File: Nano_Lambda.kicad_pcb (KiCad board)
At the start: 2 copper layers, 22.2 x 47 mm, 70 parts, among them IC1 LMV321?M5, IC2 LM4041DBZ, J1 +12_IN, J10 PD3, J11 GP3, J12 DAC1, J13 DAC2, J14 Out1, J2 GND, J3 +12V_NL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

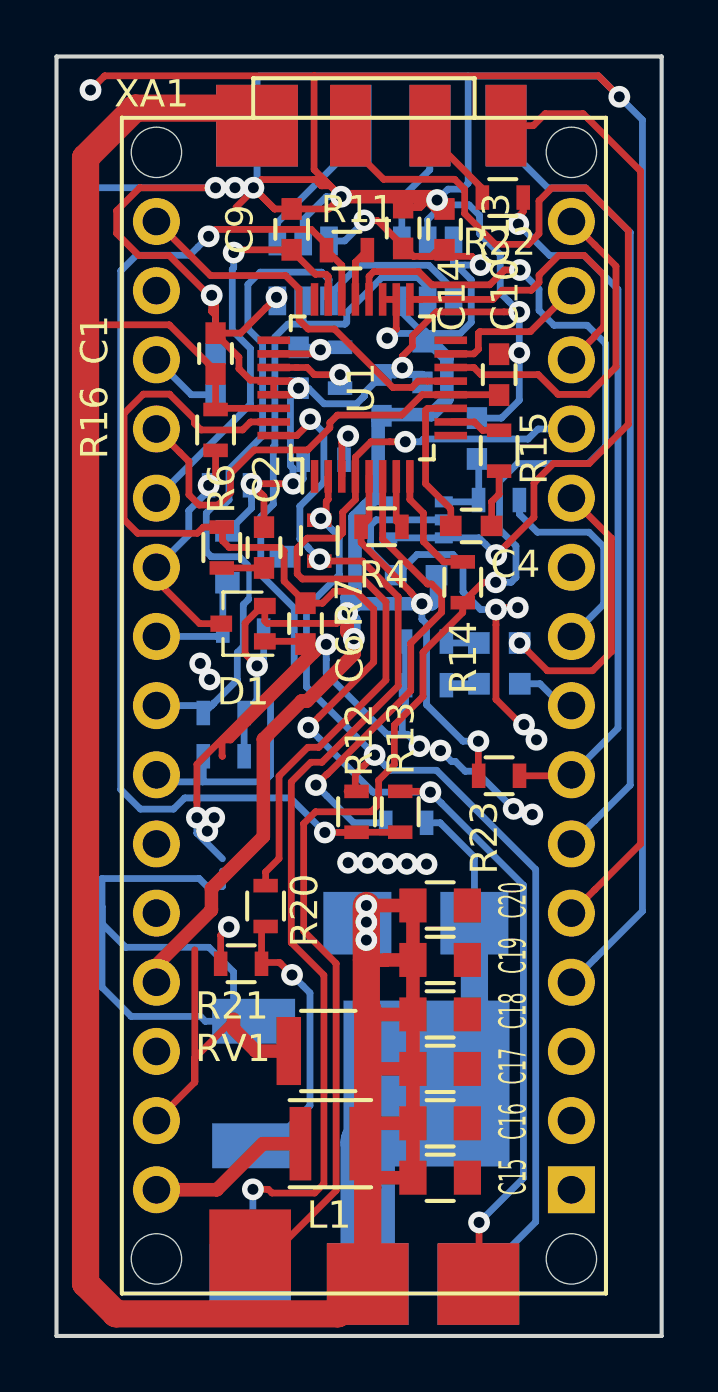
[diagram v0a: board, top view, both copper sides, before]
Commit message: Change to Version 0.9b
Changed wrong CJ125 Footprint to Footprint with 0.8mm pitch.
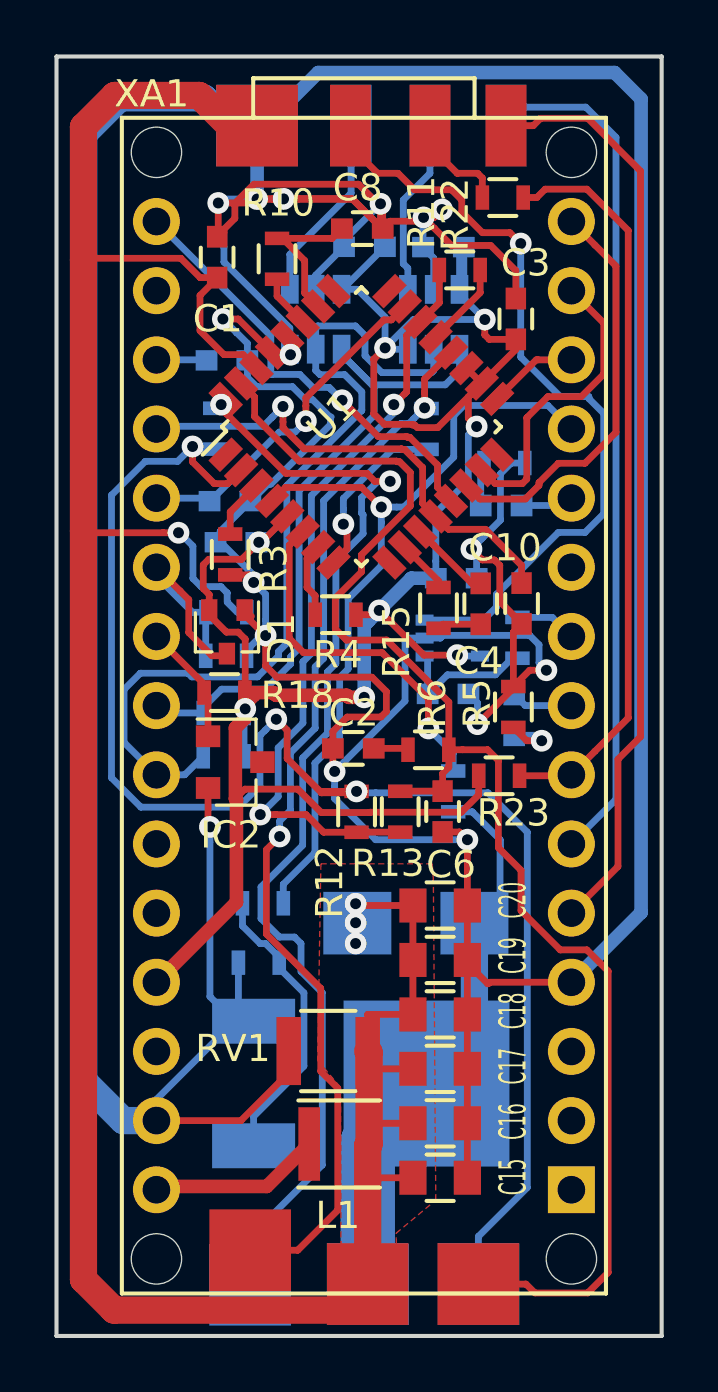
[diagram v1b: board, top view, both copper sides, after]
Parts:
- C13, C14, C9, R14, R16, R20, R21, R7: moved to B.Cu
- C3, C8, IC2, R10, R18, R3, R5: moved to F.Cu
- U1: footprint Housings_QFP:LQFP-32_5x5mm_Pitch0.5mm -> Housings_QFP:LQFP-32_7x7mm_Pitch0.8mm
- moved R6 10.6 mm to (173.7, 81.3), turned to 180 degrees
- moved C9 10.2 mm to (166.4, 72.2), turned to 0 degrees
- moved C5 9.53 mm to (166.6, 73.7), turned to 180 degrees
- moved C12 9.44 mm to (174.4, 79.3), turned to 180 degrees
- moved C6 8.54 mm to (174.2, 83.6)
- moved C10 8.45 mm to (177.1, 76.0), turned to 270 degrees
- moved C2 8.07 mm to (170.9, 81.3), turned to 180 degrees
- moved IC2 7.58 mm to (166.6, 81.8)
- moved R2 7.16 mm to (176.5, 70.8), turned to 180 degrees
- moved R16 6.71 mm to (166.3, 76.3), turned to 0 degrees
- moved R17 6.26 mm to (166.2, 77.9)
- moved R15 6.19 mm to (174.1, 76.1)
- moved R14 5.78 mm to (173.6, 69.6), turned to 90 degrees
- moved C3 5.67 mm to (176.9, 65.5)
- moved C8 5.62 mm to (171.2, 62.2), turned to 180 degrees
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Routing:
- net /IA: track 38.2 -> 57.0 mm, vias 2 -> 3
- net /VM: track 56.0 -> 39.4 mm
- net Net-(R11-Pad1): track 41.0 -> 28.1 mm
- net /LS_SS: track 11.8 -> 3.32 mm
- net /LED_1: track 10.4 -> 1.94 mm, vias 1 -> 0
- net +5V: track 79.5 -> 86.4 mm
- net /SDA: track 31.3 -> 25.2 mm
- net /WBL: track 8.27 -> 2.27 mm
- net /LS_MOSI: track 5.74 -> 11.2 mm
- net /Out1: track 34.1 -> 29.0 mm
- net /DIAHD: track 17.4 -> 13.2 mm
- net GND: track 256.7 -> 253.3 mm, vias 35 -> 16
- net /UA: track 15.5 -> 12.6 mm
- net Net-(C4-Pad1): track 5.58 -> 3.01 mm
- net Net-(C12-Pad2): track 2.83 -> 5.28 mm
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- added copper zone on F.Cu, net /+12V_NL
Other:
- board text added: "Nano Lambda Shield v0.9b 2018"
- board text removed: "Nano Lambda Shield v0.9 2018"

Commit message: Minor changes and new gerber files
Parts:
- moved C8 3.36 mm to (167.9, 62.2), turned to 225 degrees
- moved R14 1.37 mm to (173.5, 70.9)
- moved R11 0.69 mm to (174.5, 64.3), turned to 315 degrees
- moved R10 0.65 mm to (168.5, 63.8), turned to 225 degrees
- moved C1 0.36 mm to (165.6, 63.2)
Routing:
- net GND: track 253.3 -> 265.6 mm, vias 16 -> 20
- net +5V: track 86.4 -> 89.1 mm
- net /IA: track 57.0 -> 54.5 mm
- net /IP: track 42.3 -> 44.5 mm
- net Net-(C8-Pad2): track 5.77 -> 3.90 mm
- net Net-(R11-Pad2): track 3.15 -> 1.79 mm
- net /DIAHG: track 30.3 -> 31.1 mm
- net Net-(R11-Pad1): track 28.1 -> 27.6 mm
- net /UN: track 53.3 -> 53.9 mm

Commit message: Fabrication version 0.9b
Fabrication version 0.9b
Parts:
- moved C2 0.60 mm to (170.9, 81.9)
- moved R13 0.58 mm to (172.6, 84.2)
- moved R12 0.57 mm to (171.0, 84.2)
- moved R6 0.52 mm to (173.7, 81.9)
- moved C6 0.50 mm to (174.2, 84.1)
- moved R4 0.47 mm to (170.7, 76.4)
- moved C14 0.25 mm to (171.1, 62.9)
- turned D1 to 90 degrees
- turned R16 to 180 degrees
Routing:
- net GND: track 265.6 -> 333.0 mm, vias 20 -> 25
- net /IA: track 54.5 -> 47.7 mm, vias 3 -> 2
- net /+12V_NL: track 104.4 -> 100.9 mm
- net +5V: track 89.1 -> 90.6 mm, vias 8 -> 9
- net /UN: track 53.9 -> 55.0 mm
- net /SCL: track 33.2 -> 34.0 mm
- net /BRV: track 8.95 -> 9.59 mm

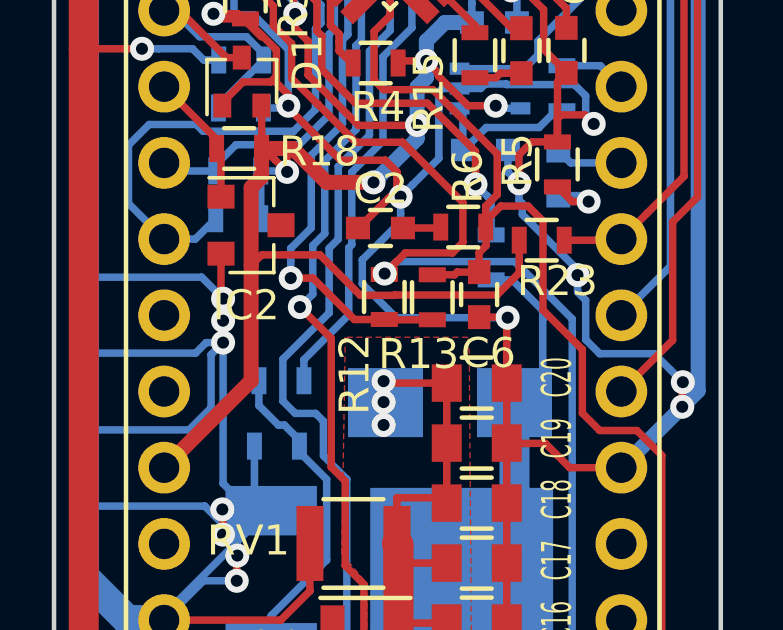
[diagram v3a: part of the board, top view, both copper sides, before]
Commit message: Diode u4 wrong direction
Swapped pin numbers on Diode MURS120 symbol in schematic. Changed pin 1
to 2 and 2 to 1
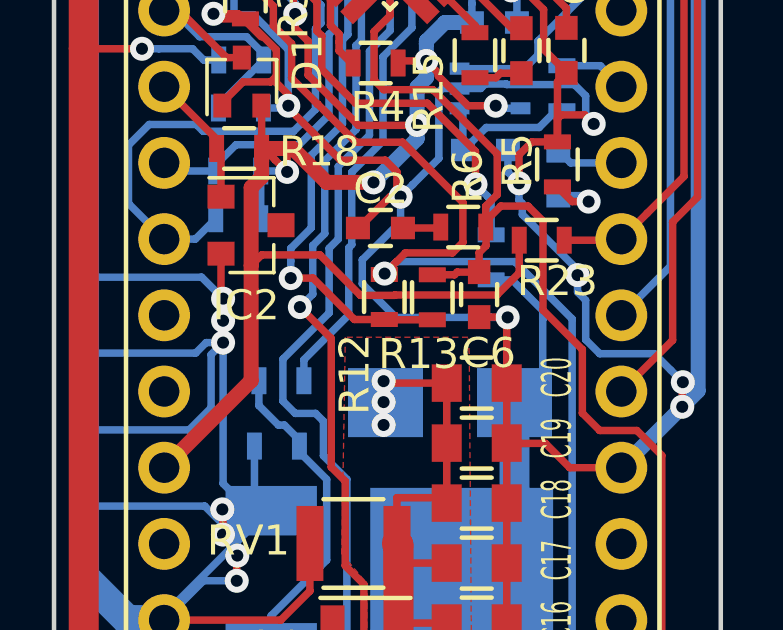
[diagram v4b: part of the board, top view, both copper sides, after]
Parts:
- turned U4 to 0 degrees
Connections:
- U4 pad 1: /NL_HEATER -> /+12V_NL
- U4 pad 2: /+12V_NL -> /NL_HEATER
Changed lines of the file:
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@@
   )
   (module Diodes_SMD:SMB_Standard (layer B.Cu)
-    (at 173.219 87.71 180)
+    (at 173.219 87.71)
     (descr "Diode SMB Standard")
     (tags "Diode SMB Standard")
     (attr smd)
-    (fp_text reference U4 (at -0.078 0.53 90) (layer B.SilkS)
-      (effects (font (size 1 1) (thickness 0.15)) (justify mirror))
-    )
-    (fp_text value MURS120 (at 0.05 -4.7 180) (layer B.Fab) hide
+    (fp_text reference U4 (at -0.078 0.53 -90) (layer B.SilkS)
+      (effects (font (size 1 1) (thickness 0.15)) (justify mirror))
+    )
+    (fp_text value MURS120 (at 0.05 -4.7) (layer B.Fab) hide
       (effects (font (size 1 1) (thickness 0.15)) (justify mirror))
     )
@@
     (fp_line (start 2.3 -2) (end -2.3 -2) (layer B.Fab) (width 0.1))
     (fp_line (start -3.55 2.15) (end -3.55 -2.15) (layer B.SilkS) (width 0.12))
-    (pad 2 smd rect (at 2.15 0 180) (size 2.5 2.3) (layers B.Cu B.Paste B.Mask)
-      (net 1 /+12V_NL))
-    (pad 1 smd rect (at -2.15 0 180) (size 2.5 2.3) (layers B.Cu B.Paste B.Mask)
+    (pad 2 smd rect (at 2.15 0) (size 2.5 2.3) (layers B.Cu B.Paste B.Mask)
       (net 24 /NL_HEATER))
+    (pad 1 smd rect (at -2.15 0) (size 2.5 2.3) (layers B.Cu B.Paste B.Mask)
+      (net 1 /+12V_NL))
     (model Diodes_SMD.3dshapes/SMB_Standard.wrl
       (at (xyz 0 0 0))
@@
   (segment (start 167.754301 77.89) (end 167.830001 77.8143) (width 0.25) (layer B.Cu) (net 2))
   (segment (start 166.02 74.78) (end 166.665685 74.78) (width 0.25) (layer B.Cu) (net 2))
-  (via (at 175.14 84.88) (size 0.8) (drill 0.4) (layers F.Cu B.Cu) (net 2))
-  (segment (start 175.11 87.06) (end 175.11 84.91) (width 0.25) (layer F.Cu) (net 2))
-  (segment (start 175.11 84.91) (end 175.14 84.88) (width 0.25) (layer F.Cu) (net 2))
-  (segment (start 175.12 84.86) (end 175.14 84.88) (width 0.25) (layer F.Cu) (net 2))
-  (segment (start 174.19 84.86) (end 175.12 84.86) (width 0.25) (layer F.Cu) (net 2))
   (segment (start 171.443005 80.589999) (end 171.443005 80.72869) (width 0.25) (layer F.Cu) (net 2))
   (via (at 171.573077 80.845367) (size 0.8) (drill 0.4) (layers F.Cu B.Cu) (net 2))
@@
   (segment (start 169.57 79.63) (end 167.7 77.76) (width 0.25) (layer F.Cu) (net 2))
   (segment (start 171.443005 80.589999) (end 171.45 80.583004) (width 0.25) (layer F.Cu) (net 2))
-  (segment (start 171.426998 84.88) (end 170.294999 83.748001) (width 0.25) (layer B.Cu) (net 2))
-  (segment (start 170.294999 83.748001) (end 170.294999 82.951999) (width 0.25) (layer B.Cu) (net 2))
-  (segment (start 171.573077 81.673921) (end 171.573077 81.411052) (width 0.25) (layer B.Cu) (net 2))
-  (segment (start 175.14 84.88) (end 171.426998 84.88) (width 0.25) (layer B.Cu) (net 2))
-  (segment (start 170.294999 82.951999) (end 171.573077 81.673921) (width 0.25) (layer B.Cu) (net 2))
-  (segment (start 171.573077 81.411052) (end 171.573077 80.845367) (width 0.25) (layer B.Cu) (net 2))
   (via (at 175.519327 80.4) (size 0.8) (drill 0.4) (layers F.Cu B.Cu) (net 2))
   (segment (start 175.15 80.030673) (end 175.519327 80.4) (width 0.25) (layer B.Cu) (net 2))
@@
   (segment (start 166.39 62.005) (end 166.5 61.895) (width 0.25) (layer F.Cu) (net 2))
   (segment (start 166.315 63.28) (end 166.39 63.205) (width 0.25) (layer F.Cu) (net 2))
+  (segment (start 170.294999 82.951999) (end 170.294999 83.748001) (width 0.25) (layer B.Cu) (net 2))
+  (segment (start 171.573077 80.845367) (end 171.573077 81.673921) (width 0.25) (layer B.Cu) (net 2))
+  (segment (start 170.294999 83.748001) (end 171.416998 84.87) (width 0.25) (layer B.Cu) (net 2))
+  (segment (start 174.574315 84.87) (end 175.14 84.87) (width 0.25) (layer B.Cu) (net 2))
+  (segment (start 171.573077 81.673921) (end 170.294999 82.951999) (width 0.25) (layer B.Cu) (net 2))
+  (segment (start 175.13 84.86) (end 175.14 84.87) (width 0.25) (layer F.Cu) (net 2))
+  (segment (start 174.19 84.86) (end 175.13 84.86) (width 0.25) (layer F.Cu) (net 2))
+  (segment (start 175.11 87.06) (end 175.11 84.9) (width 0.25) (layer F.Cu) (net 2))
+  (segment (start 175.11 84.9) (end 175.14 84.87) (width 0.25) (layer F.Cu) (net 2))
+  (segment (start 171.416998 84.87) (end 174.574315 84.87) (width 0.25) (layer B.Cu) (net 2))
+  (via (at 175.14 84.87) (size 0.8) (drill 0.4) (layers F.Cu B.Cu) (net 2))
   (segment (start 172.88 81.89) (end 172.91 81.86) (width 0.25) (layer F.Cu) (net 3))
   (segment (start 171.65 81.89) (end 172.88 81.89) (width 0.25) (layer F.Cu) (net 3))
